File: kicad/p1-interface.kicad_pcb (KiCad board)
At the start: 2 copper layers, 18 x 29.5 mm, 6 parts, among them J1 P1 Connector, J2 Conn_01x06, J3 Conn_01x02, Q1 BC847

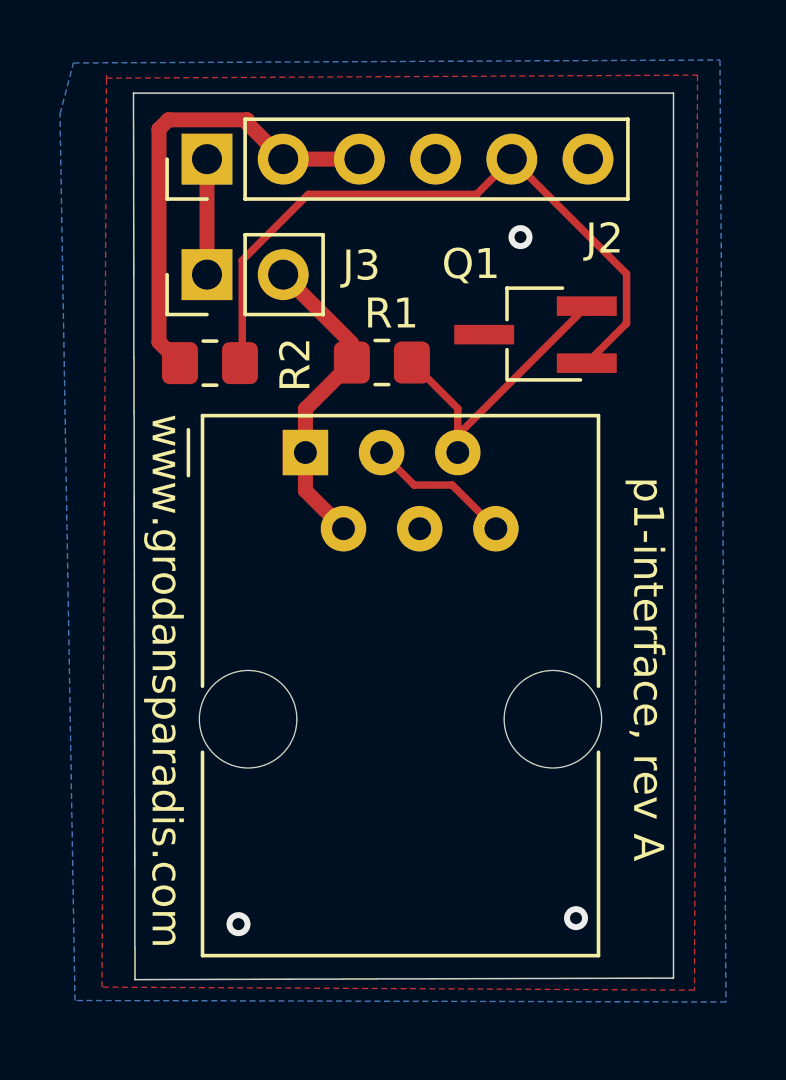
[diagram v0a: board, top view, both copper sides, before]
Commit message: Updated images and readme for rev B
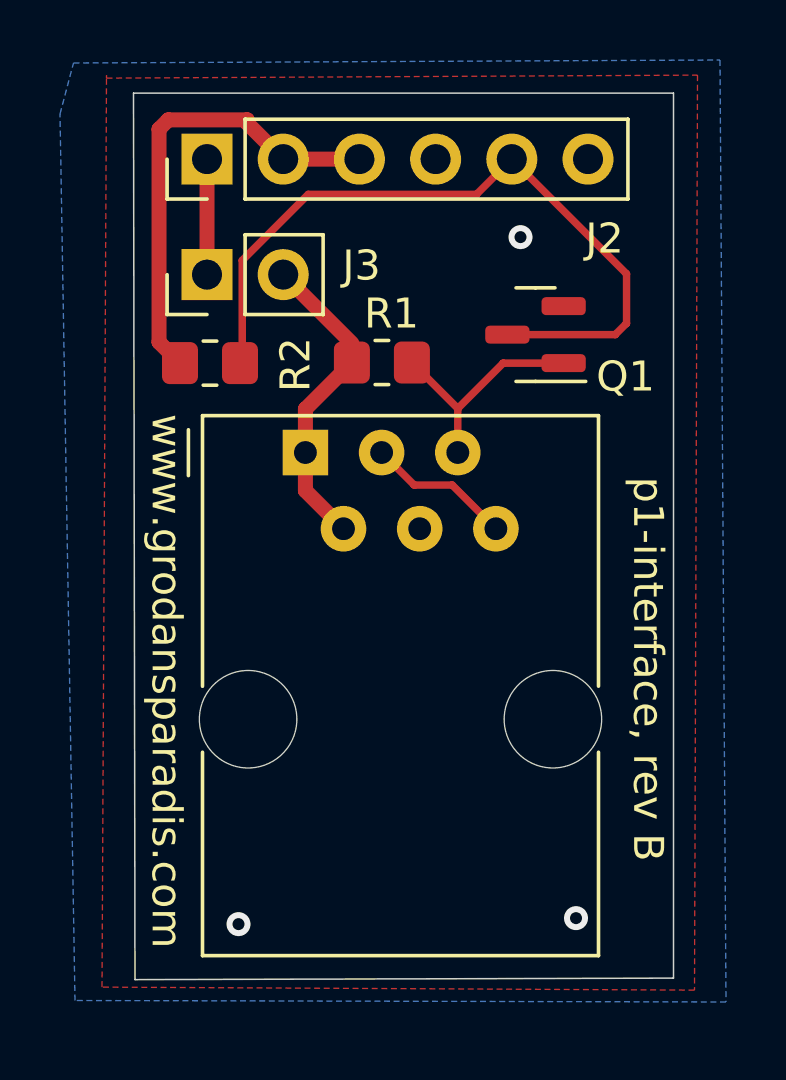
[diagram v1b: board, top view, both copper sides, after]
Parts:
- Q1: footprint Package_TO_SOT_SMD:TSOT-23_HandSoldering -> Package_TO_SOT_SMD:SOT-23
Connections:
- Q1 pad 1: /rx -> Net-(J1-Pad5)
- Q1 pad 2: Net-(J1-Pad5) -> GND
- Q1 pad 3: GND -> /rx
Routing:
- net Net-(J1-Pad5): track 10.3 -> 7.79 mm
- net /rx: track 22.8 -> 25.0 mm
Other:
- board text added: "p1-interface, rev B"
- board text removed: "p1-interface, rev A"
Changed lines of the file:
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@@
     )
   )
-  (footprint "Package_TO_SOT_SMD:TSOT-23_HandSoldering" (layer "F.Cu")
+  (footprint "Package_TO_SOT_SMD:SOT-23" (layer "F.Cu")
     (at 139.7 68.6 180)
-    (descr "5-pin TSOT23 package, http://cds.linear.com/docs/en/packaging/SOT_5_05-08-1635.pdf")
-    (tags "TSOT-23 Hand-soldering")
+    (descr "SOT, 3 Pin (https://www.jedec.org/system/files/docs/to-236h.pdf variant AB), generated with kicad-footprint-generator ipc_gullwing_generator.py")
+    (tags "SOT TO_SOT_SMD")
     (property "Sheetfile" "p1-interface.kicad_sch")
     (property "Sheetname" "")
     (attr smd)
-    (fp_text reference "Q1" (at 2.15 2.35 180) (layer "F.SilkS")
-      (effects (font (size 1 1) (thickness 0.15)))
-    )
-    (fp_text value "BC847" (at 0 2.5) (layer "F.Fab") hide
-      (effects (font (size 1 1) (thickness 0.15)))
-    )
-    (fp_text user "${REFERENCE}" (at 0 0 90) (layer "F.Fab")
-      (effects (font (size 0.5 0.5) (thickness 0.075)))
-    )
-    (fp_line (start 0.95 1.55) (end -0.9 1.55) (layer "F.SilkS") (width 0.12))
-    (fp_line (start 0.95 0.5) (end 0.95 1.55) (layer "F.SilkS") (width 0.12))
-    (fp_line (start 0.95 -1.5) (end 0.95 -0.5) (layer "F.SilkS") (width 0.12))
-    (fp_line (start 0.93 -1.51) (end -1.5 -1.51) (layer "F.SilkS") (width 0.12))
-    (fp_line (start 2.96 1.7) (end -2.96 1.7) (layer "F.CrtYd") (width 0.05))
-    (fp_line (start -2.96 -1.7) (end -2.96 1.7) (layer "F.CrtYd") (width 0.05))
-    (fp_line (start 2.96 1.7) (end 2.96 -1.7) (layer "F.CrtYd") (width 0.05))
-    (fp_line (start -2.96 -1.7) (end 2.96 -1.7) (layer "F.CrtYd") (width 0.05))
-    (fp_line (start -0.88 -1) (end -0.43 -1.45) (layer "F.Fab") (width 0.1))
-    (fp_line (start -0.88 -1) (end -0.88 1.45) (layer "F.Fab") (width 0.1))
-    (fp_line (start 0.88 -1.45) (end 0.88 1.45) (layer "F.Fab") (width 0.1))
-    (fp_line (start 0.88 1.45) (end -0.88 1.45) (layer "F.Fab") (width 0.1))
-    (fp_line (start 0.88 -1.45) (end -0.43 -1.45) (layer "F.Fab") (width 0.1))
-    (pad "1" smd rect (at -1.71 -0.95 180) (size 2 0.65) (layers "F.Cu" "F.Paste" "F.Mask")
+    (fp_text reference "Q1" (at -3 -1.4 180) (layer "F.SilkS")
+      (effects (font (size 1 1) (thickness 0.15)))
+    )
+    (fp_text value "BC847" (at 0 2.4 180) (layer "F.Fab") hide
+      (effects (font (size 1 1) (thickness 0.15)))
+    )
+    (fp_text user "${REFERENCE}" (at 0 0 180) (layer "F.Fab")
+      (effects (font (size 0.32 0.32) (thickness 0.05)))
+    )
+    (fp_line (start 0 -1.56) (end 0.65 -1.56) (layer "F.SilkS") (width 0.12))
+    (fp_line (start 0 1.56) (end -0.65 1.56) (layer "F.SilkS") (width 0.12))
+    (fp_line (start 0 1.56) (end 0.65 1.56) (layer "F.SilkS") (width 0.12))
+    (fp_line (start 0 -1.56) (end -1.675 -1.56) (layer "F.SilkS") (width 0.12))
+    (fp_line (start -1.92 1.7) (end 1.92 1.7) (layer "F.CrtYd") (width 0.05))
+    (fp_line (start 1.92 1.7) (end 1.92 -1.7) (layer "F.CrtYd") (width 0.05))
+    (fp_line (start 1.92 -1.7) (end -1.92 -1.7) (layer "F.CrtYd") (width 0.05))
+    (fp_line (start -1.92 -1.7) (end -1.92 1.7) (layer "F.CrtYd") (width 0.05))
+    (fp_line (start 0.65 -1.45) (end 0.65 1.45) (layer "F.Fab") (width 0.1))
+    (fp_line (start 0.65 1.45) (end -0.65 1.45) (layer "F.Fab") (width 0.1))
+    (fp_line (start -0.325 -1.45) (end 0.65 -1.45) (layer "F.Fab") (width 0.1))
+    (fp_line (start -0.65 1.45) (end -0.65 -1.125) (layer "F.Fab") (width 0.1))
+    (fp_line (start -0.65 -1.125) (end -0.325 -1.45) (layer "F.Fab") (width 0.1))
+    (pad "1" smd roundrect (at -0.9375 -0.95 180) (size 1.475 0.6) (layers "F.Cu" "F.Paste" "F.Mask") (roundrect_rratio 0.25)
+      (net 4 "Net-(J1-Pad5)") (pinfunction "B") (pintype "input"))
+    (pad "2" smd roundrect (at -0.9375 0.95 180) (size 1.475 0.6) (layers "F.Cu" "F.Paste" "F.Mask") (roundrect_rratio 0.25)
+      (net 2 "GND") (pinfunction "E") (pintype "passive"))
+    (pad "3" smd roundrect (at 0.9375 0 180) (size 1.475 0.6) (layers "F.Cu" "F.Paste" "F.Mask") (roundrect_rratio 0.25)
       (net 8 "/rx") (pinfunction "C") (pintype "passive"))
-    (pad "2" smd rect (at -1.71 0.95 180) (size 2 0.65) (layers "F.Cu" "F.Paste" "F.Mask")
-      (net 4 "Net-(J1-Pad5)") (pinfunction "B") (pintype "input"))
-    (pad "3" smd rect (at 1.71 0 180) (size 2 0.65) (layers "F.Cu" "F.Paste" "F.Mask")
-      (net 2 "GND") (pinfunction "E") (pintype "passive"))
-    (model "${KICAD6_3DMODEL_DIR}/Package_TO_SOT_SMD.3dshapes/TSOT-23.wrl"
+    (model "${KICAD6_3DMODEL_DIR}/Package_TO_SOT_SMD.3dshapes/SOT-23.wrl"
       (offset (xyz 0 0 0))
       (scale (xyz 1 1 1))
@@
     (effects (font (size 1 1) (thickness 0.2)))
   )
-  (gr_text "p1-interface, rev A" (at 143.45 79.75 270) (layer "F.SilkS")
+  (gr_text "p1-interface, rev B" (at 143.45 79.75 270) (layer "F.SilkS")
     (effects (font (size 1 1) (thickness 0.15)))
   )
@@
   (via (at 141.05 88.05) (size 0.8) (drill 0.4) (layers "F.Cu" "B.Cu") (free) (net 2))
   (segment (start 137.11 71.06) (end 137.11 72.53) (width 0.25) (layer "F.Cu") (net 4))
-  (segment (start 137.11 71.95) (end 137.11 72.53) (width 0.25) (layer "F.Cu") (net 4))
+  (segment (start 140.6375 69.55) (end 138.62 69.55) (width 0.25) (layer "F.Cu") (net 4))
   (segment (start 135.58 69.53) (end 137.11 71.06) (width 0.25) (layer "F.Cu") (net 4))
-  (segment (start 141.41 67.65) (end 137.11 71.95) (width 0.25) (layer "F.Cu") (net 4))
+  (segment (start 138.62 69.55) (end 137.11 71.06) (width 0.25) (layer "F.Cu") (net 4))
   (segment (start 128.75 62.75) (end 128.75 66.6) (width 0.5) (layer "F.Cu") (net 5))
   (segment (start 127.15 61.750978) (end 127.15 68.85) (width 0.5) (layer "F.Cu") (net 6))
@@
   (segment (start 129.924511 69.475489) (end 129.924511 66.125489) (width 0.25) (layer "F.Cu") (net 8))
   (segment (start 132.125489 63.924511) (end 137.735489 63.924511) (width 0.25) (layer "F.Cu") (net 8))
-  (segment (start 141.41 69.55) (end 142.734511 68.225489) (width 0.25) (layer "F.Cu") (net 8))
+  (segment (start 142.734511 68.225489) (end 142.36 68.6) (width 0.25) (layer "F.Cu") (net 8))
+  (segment (start 142.36 68.6) (end 138.7625 68.6) (width 0.25) (layer "F.Cu") (net 8))
   (segment (start 142.734511 68.225489) (end 142.734511 66.574511) (width 0.25) (layer "F.Cu") (net 8))
   (zone (net 2) (net_name "GND") (layer "F.Cu") (hatch edge 0.508)
